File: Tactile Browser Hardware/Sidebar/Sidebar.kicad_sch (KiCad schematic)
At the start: 0 parts

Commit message: I2C
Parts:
- added A1: Arduino_Nano_v3.x, Module:Arduino_Nano, symbol MCU_Module:Arduino_Nano_v3.x
- added Buck_converter: LM2596S-5, Package_TO_SOT_SMD:TO-263-5_TabPin3, symbol Regulator_Switching:LM2596S-5
- added R1, R2: R, symbol Device:R
- added SW1, SW2, SW3, SW4, SW5, SW6, SW7, SW8: SW_Push, symbol Switch:SW_Push
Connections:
- new net 5V: A1.27 (+5V)
- new net GND: A1.29 (GND), A1.4 (GND)
- new net SCL: A1.24 (A5)
- new net SDA: A1.23 (A4)

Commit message: more sidebar progress
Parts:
- removed Buck_converter: LM2596S-5, Package_TO_SOT_SMD:TO-263-5_TabPin3, symbol Regulator_Switching:LM2596S-5
- removed SW8: SW_Push, symbol Switch:SW_Push
- added J1, J2: Conn_01x02_Pin, symbol Connector:Conn_01x02_Pin
- added J3: Barrel_Jack, symbol Connector:Barrel_Jack
- added SW9: RotaryEncoder, symbol Device:RotaryEncoder
- added U1: XL4015, Package_TO_SOT_SMD:TO-263-5_TabPin3, symbol Regulator_Switching:XL4015
- renumbered R1 to 4.7k_ohm, R2 to 4.7k_ohm2, SW2 to Down, SW3 to Left, SW4 to Right, SW1 to Up, SW5 to power_button
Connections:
- net 5V: now also 4.7k_ohm.1, 4.7k_ohm2.2
- net GND: now also SW9.C, U1.1 (GND)
- net SCL: now also 4.7k_ohm2.1, J1.1 (Pin_1)
- net SDA: now also 4.7k_ohm.2, J1.2 (Pin_2)
- net SW5_in: now reaches power_button.1
- net SW5_in: now also A1.19 (A0)
- net SW5_out: now reaches power_button.2
- net SW5_out: now also A1.20 (A1)
- net SW6_in: now reaches SW6.1
- net SW6_in: now also A1.21 (A2)
- net SW6_out: now reaches SW6.2
- net SW6_out: now also A1.22 (A3)
- net SW3_in: now reaches Left.1
- net SW3_in: now also A1.11 (D8)
- net SW3_out: now reaches Left.2
- net SW3_out: now also A1.14 (D11)
- net SW2_out: now reaches A1.10 (D7)
- net SW2_out: now also Down.2
- net PWM1: now reaches A1.12 (D9)
- net PWM1: now also J2.1 (Pin_1)
- net PWM2: now reaches A1.13 (D10)
- net PWM2: now also J2.2 (Pin_2)
- net SW4_in: now reaches A1.15 (D12)
- net SW4_in: now also Right.1
- net SW4_out: now reaches A1.16 (D13)
- net SW4_out: now also Right.2
- net SW7_in: now reaches A1.25 (A6)
- net SW7_in: now also SW7.1
- net SW7_out: now reaches A1.26 (A7)
- net SW7_out: now also SW7.2
- net RE1: now reaches A1.5 (D2)
- net RE1: now also SW9.A
- net RE2: now reaches A1.6 (D3)
- net RE2: now also SW9.B
- net SW1_in: now reaches A1.7 (D4)
- net SW1_in: now also Up.1
- net SW1_out: now reaches A1.8 (D5)
- net SW1_out: now also Up.2
- net SW2_in: now reaches A1.9 (D6)
- net SW2_in: now also Down.1
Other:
- moved on the sheet: 4.7k_ohm, 4.7k_ohm2, Down, Left, Right, SW6, SW7, Up, power_button

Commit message: sidebar progress
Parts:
- added AudioSpeed: RotaryEncoder, symbol Device:RotaryEncoder
- added U2: 74HC595, symbol 74xx:74HC595
- renumbered SW9 to Volume
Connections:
- net 5V: now also U2.10 (~{SRCLR}), U2.16 (VCC)
- net GND: now also AudioSpeed.C, U2.13 (~{OE}), U2.8 (GND)
- net PWM1: now also A1.8 (D5); no longer A1.12 (D9)
- net PWM2: now also A1.12 (D9); no longer A1.13 (D10)
- net SW1_in: now also A1.10 (D7); no longer A1.7 (D4)
- net SW1_out: now also A1.11 (D8); no longer A1.8 (D5)
- net SW2_in: now also A1.19 (A0); no longer A1.9 (D6)
- net SW2_out: now also A1.20 (A1); no longer A1.10 (D7)
- net SW3_in: now also A1.21 (A2); no longer A1.11 (D8)
- net SW3_out: now also A1.22 (A3); no longer A1.14 (D11)
- net SW4_in: now also A1.25 (A6); no longer A1.15 (D12)
- net SW4_out: now also A1.26 (A7); no longer A1.16 (D13)
- net SW5_in: now also U2.15 (QA); no longer A1.19 (A0)
- net SW5_out: now also U2.1 (QB); no longer A1.20 (A1)
- net SW6_in: now also U2.2 (QC); no longer A1.21 (A2)
- net SW6_out: now also U2.3 (QD); no longer A1.22 (A3)
- net SW7_in: now also U2.4 (QE); no longer A1.25 (A6)
- net SW7_out: now also U2.5 (QF); no longer A1.26 (A7)
- net 12V: now reaches U1.5 (VIN)
- new net AS1: A1.7 (D4), AudioSpeed.A
- new net AS2: A1.9 (D6), AudioSpeed.B
- new net CLOCK: A1.16 (D13), U2.11 (SRCLK)
- new net DATA: A1.14 (D11), U2.14 (SER)
- new net LATCH: A1.13 (D10), U2.12 (RCLK)

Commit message: electrical safety
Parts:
- removed J3: Barrel_Jack, symbol Connector:Barrel_Jack
- removed U1: XL4015, Package_TO_SOT_SMD:TO-263-5_TabPin3, symbol Regulator_Switching:XL4015
- added 100k, R220: R, symbol Device:R
- added 6,800-10,000uf: C_US, symbol Device:C_US
- added F_20A: Fuse, symbol Device:Fuse
- added J3: Barrel_Jack_Switch, symbol Connector:Barrel_Jack_Switch
- added Kill_Switch_DC: SW_SPST, symbol Switch:SW_SPST
- added Q1: Q_PMOS_SGD, symbol Transistor_FET:Q_PMOS_SGD
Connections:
- net 12V: now also 6,800-10,000uf.1, Q1.1 (S)
- net GND: now also 6,800-10,000uf.2, J3.2
- net D12_mosfet: now reaches A1.15 (D12)
- net D12_mosfet: now also R220.1
- new net: 100k.1, Q1.2 (G), R220.2
- new net: 100k.2, Kill_Switch_DC.2 (B), Q1.3 (D)
- new net: F_20A.1, J3.1
- new net: F_20A.2, Kill_Switch_DC.1 (A)

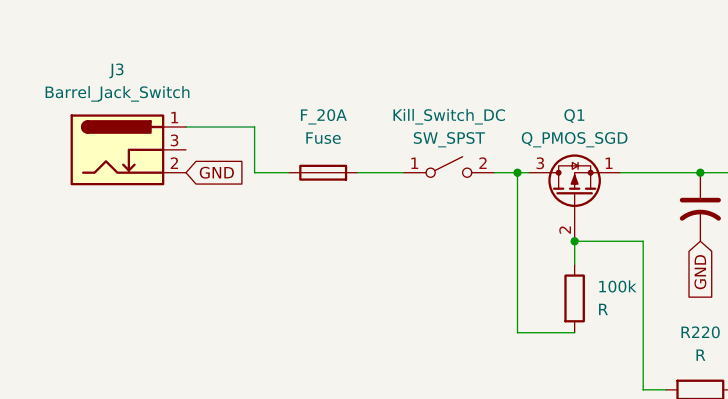
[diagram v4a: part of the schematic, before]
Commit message: updated solenoid/keyswitch connectors
for ease of manufacturing
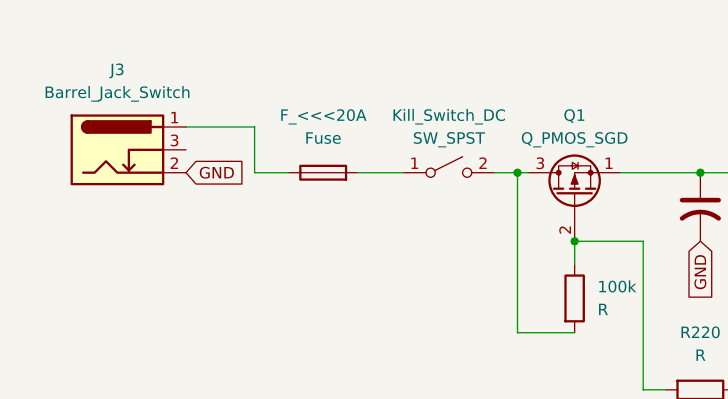
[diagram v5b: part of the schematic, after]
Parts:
- renumbered F_20A to F_<<<20A
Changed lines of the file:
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@@
 		(dnp no)
 		(fields_autoplaced yes)
-		(property "Reference" "F_20A"
+		(property "Reference" "F_<<<20A"
 			(at 45.72 43.18 90)
 			(effects
@@
 			(project ""
 				(path "/16cfaf40-0992-40a8-a734-5ca99128006a"
-					(reference "F_20A")
+					(reference "F_<<<20A")
 					(unit 1)
 				)

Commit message: sidebar updates
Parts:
- removed 100k, R220: R, symbol Device:R
- removed Q1: Q_PMOS_SGD, symbol Transistor_FET:Q_PMOS_SGD
- removed U2: 74HC595, symbol 74xx:74HC595
- added SW10, SW11, SW12, SW8, SW9: SW_Push, symbol Switch:SW_Push
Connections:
- net 12V: now also Kill_Switch_DC.2 (B)
- net SW1_in: no longer A1.10 (D7)
- net SW2_in: no longer A1.19 (A0)
- net SW3_in: no longer A1.21 (A2)
- net SW4_in: no longer A1.25 (A6)
- net CLOCK: no longer names the net of A1.16 (D13)
- net DATA: no longer names the net of A1.14 (D11)
- net LATCH: no longer names the net of A1.13 (D10)
- net SW1_out: no longer names the net of Up.2
- net SW1_out: no longer A1.11 (D8)
- net SW2_out: no longer names the net of A1.20 (A1)
- net SW2_out: no longer Down.2
- net SW3_out: no longer names the net of Left.2
- net SW3_out: no longer A1.22 (A3)
- net SW4_out: no longer names the net of A1.26 (A7)
- net SW4_out: no longer Right.2
- net SW5_in: no longer names the net of power_button.1
- net SW5_out: no longer names the net of power_button.2
- net SW6_in: no longer names the net of SW6.1
- net SW6_out: no longer names the net of SW6.2
- net SW7_in: no longer names the net of SW7.1
- net SW7_out: no longer names the net of SW7.2
- new net Row1: A1.10 (D7)
- new net Row2: A1.11 (D8)
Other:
- moved on the sheet: 4.7k_ohm, 4.7k_ohm2, 6,800-10,000uf, A1, AudioSpeed, Down, F_<<<20A, J1, J2, J3, Kill_Switch_DC, Left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

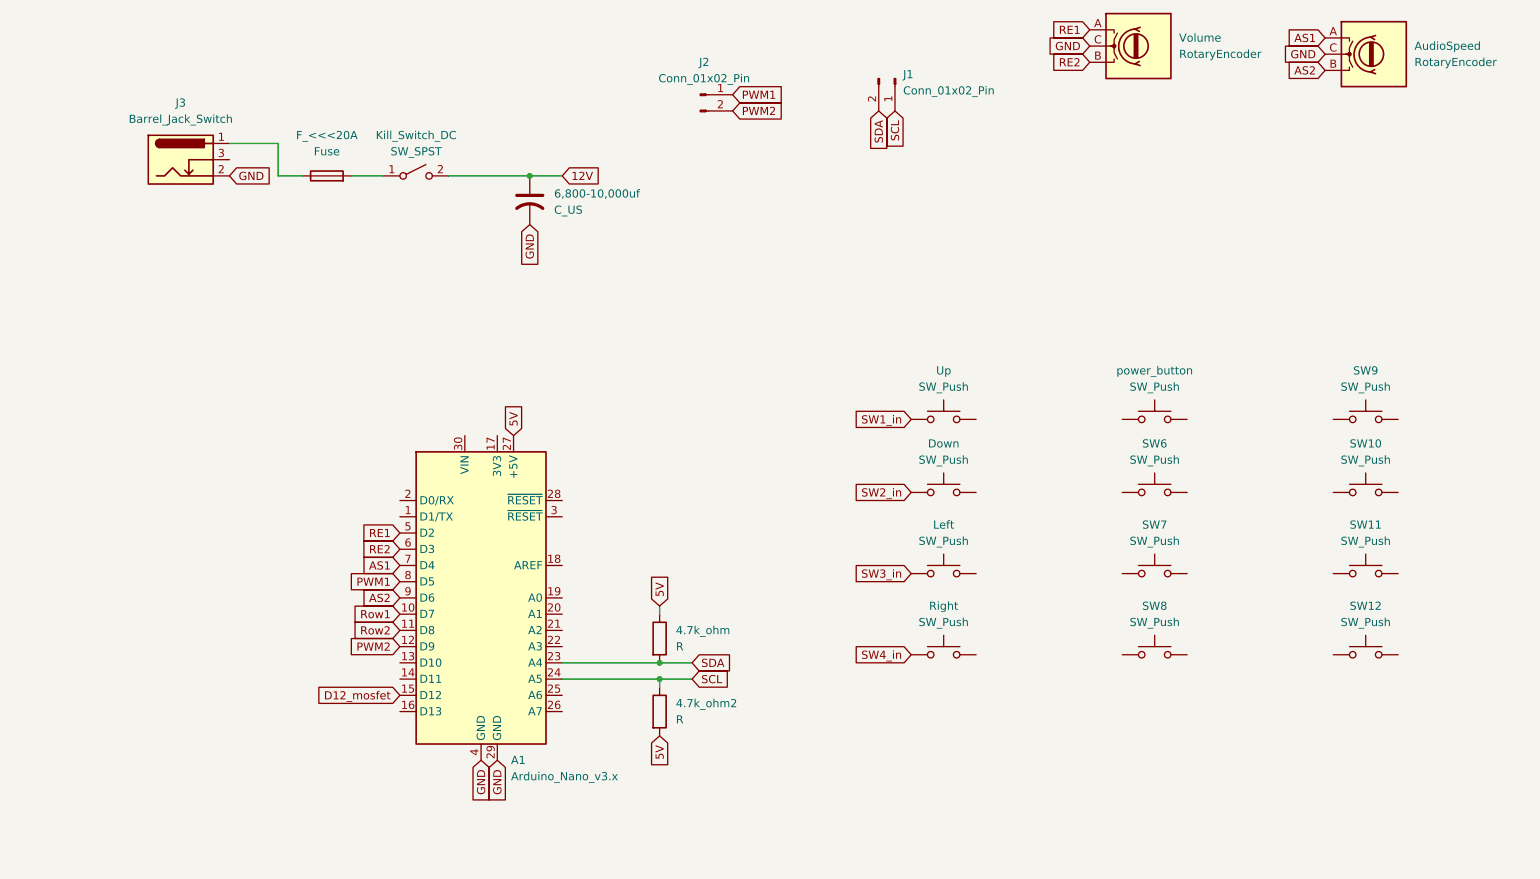
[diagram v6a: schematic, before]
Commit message: finished with sidebar schematic!
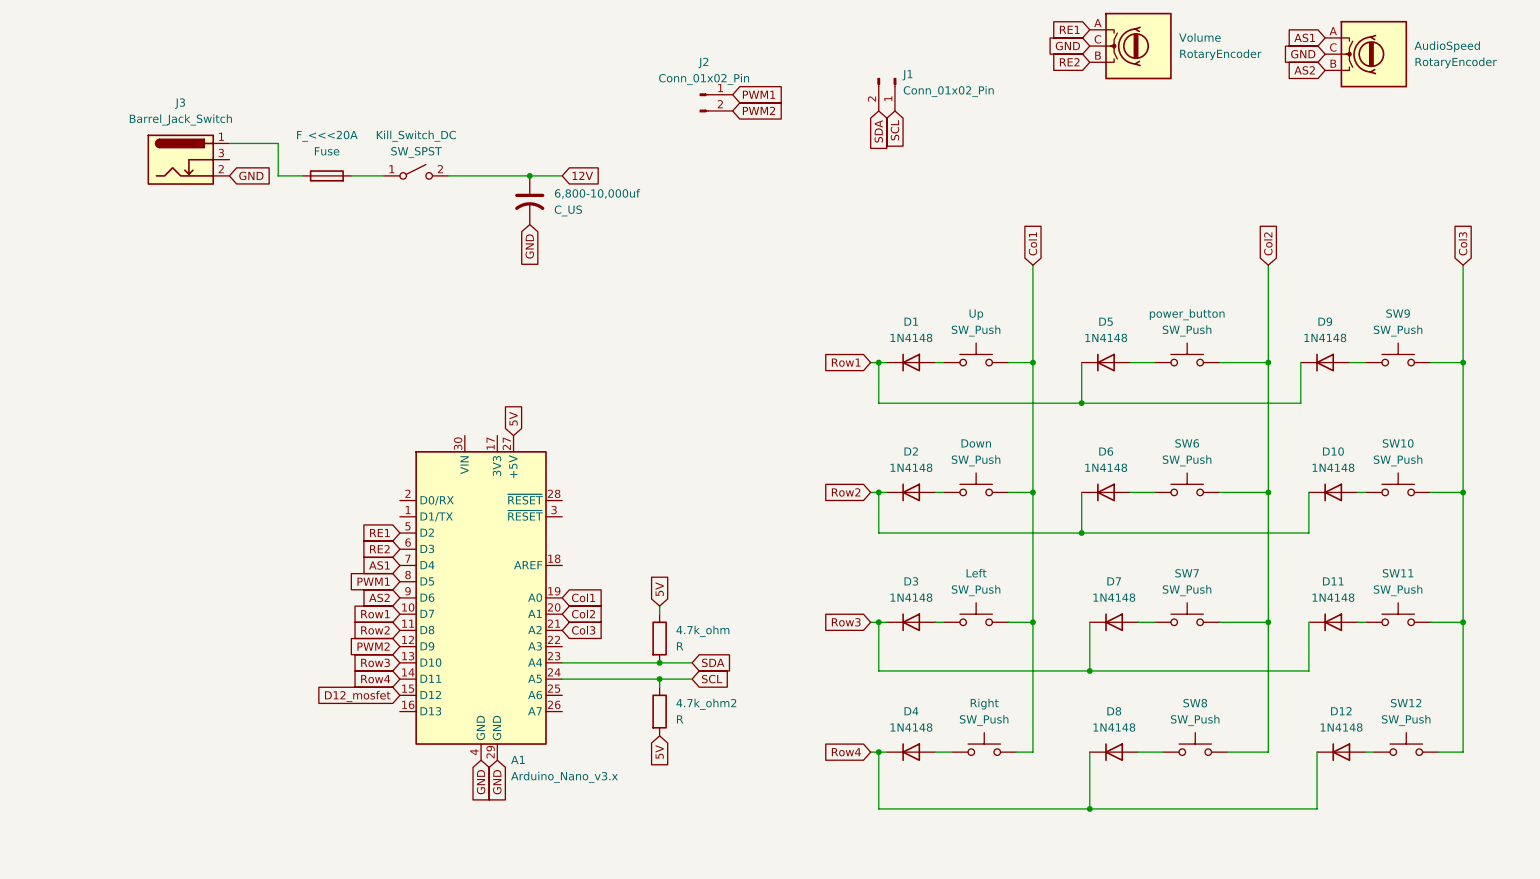
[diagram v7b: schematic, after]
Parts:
- added D1, D10, D11, D12, D2, D3, D4, D5, D6, D7, D8, D9: 1N4148, Diode_THT:D_DO-35_SOD27_P7.62mm_Horizontal, symbol Diode:1N4148
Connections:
- net Row1: now also D1.1 (K), D5.1 (K), D9.1 (K)
- net Row2: now also D10.1 (K), D2.1 (K), D6.1 (K)
- net at power_button.1: now also D5.2 (A)
- net Col2: now reaches power_button.2
- net Col2: now also A1.20 (A1), SW6.2, SW7.2, SW8.2
- net at SW11.1: now also D11.2 (A)
- net Col3: now reaches SW11.2
- net Col3: now also A1.21 (A2), SW10.2, SW12.2, SW9.2
- net at SW6.1: now also D6.2 (A)
- net Col1: now reaches Left.2
- net Col1: now also A1.19 (A0), Down.2, Right.2, Up.2
- net Row3: now reaches A1.13 (D10)
- net Row3: now also D11.1 (K), D3.1 (K), D7.1 (K)
- net Row4: now reaches A1.14 (D11)
- net Row4: now also D12.1 (K), D4.1 (K), D8.1 (K)
- net at SW10.1: now also D10.2 (A)
- net at SW12.1: now also D12.2 (A)
- net at SW8.1: now also D8.2 (A)
- net at SW7.1: now also D7.2 (A)
- net at SW9.1: now also D9.2 (A)
- net SW1_in: no longer names the net of Up.1
- net SW1_in: now also D1.2 (A)
- net SW2_in: no longer names the net of Down.1
- net SW2_in: now also D2.2 (A)
- net SW3_in: no longer names the net of Left.1
- net SW3_in: now also D3.2 (A)
- net SW4_in: no longer names the net of Right.1
- net SW4_in: now also D4.2 (A)
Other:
- moved on the sheet: Down, Left, Right, SW10, SW11, SW12, SW6, SW7, SW8, SW9, Up, power_button

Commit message: finished footprints (mostly)
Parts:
- added 1000uf25V1, 1000uf25V2: C_US, Capacitor_SMD:CP_Elec_10x12.5, symbol Device:C_US
- added J4: Conn_01x02_Pin, Connector_JST:JST_PH_B2B-PH-SM4-TB_1x02-1MP_P2.00mm_Vertical, symbol Connector:Conn_01x02_Pin
- 1000uf25V3: renamed from 6,800-10,000uf; footprint (none) -> Capacitor_SMD:CP_Elec_10x12.5
- 4.7k_ohm1: renamed from 4.7k_ohm; footprint (none) -> Resistor_SMD:R_0402_1005Metric
- 4.7k_ohm2: footprint (none) -> Resistor_SMD:R_0402_1005Metric
- AudioSpeed1: renamed from AudioSpeed; footprint (none) -> Rotary_Encoder:RotaryEncoder_Bourns_Horizontal_PEC12R-2x17F-Sxxxx
- D1, D10, D11, D12, D2, D3, D4, D5, D6, D7, D8, D9: footprint Diode_THT:D_DO-35_SOD27_P7.62mm_Horizontal -> Diode_SMD:D_SOD-123
- Down1: renamed from Down; footprint (none) -> Button_Switch_SMD:SW_SPST_EVQQ2
- Fuse1: renamed from F_<<<20A; footprint (none) -> Fuse:Fuse_0402_1005Metric_Pad0.77x0.64mm_HandSolder
- J1: footprint (none) -> Connector_JST:JST_PH_B2B-PH-SM4-TB_1x02-1MP_P2.00mm_Vertical
- J2: footprint (none) -> TerminalBlock_MetzConnect:TerminalBlock_MetzConnect_Type011_RT05503HBLC_1x03_P5.00mm_Horizontal
- J3: footprint (none) -> Connector_BarrelJack:BarrelJack_CUI_PJ-063AH_Horizontal
- Kill_Switch_DC1: renamed from Kill_Switch_DC; footprint (none) -> Button_Switch_Keyboard:SW_Cherry_MX_1.00u_PCB
- Left1: renamed from Left; footprint (none) -> Button_Switch_SMD:SW_SPST_EVQQ2
- Right1: renamed from Right; footprint (none) -> Button_Switch_SMD:SW_SPST_EVQQ2
- SW10, SW11, SW12, SW6, SW7, SW8, SW9: footprint (none) -> Button_Switch_SMD:SW_SPST_EVQQ2
- Up1: renamed from Up; footprint (none) -> Button_Switch_SMD:SW_SPST_EVQQ2
- Volume1: renamed from Volume; footprint (none) -> Rotary_Encoder:RotaryEncoder_Bourns_Horizontal_PEC12R-2x17F-Sxxxx
- power_button1: renamed from power_button; footprint (none) -> Button_Switch_SMD:SW_SPST_EVQQ2
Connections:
- net 12V: now also J2.1 (Pin_1), 1000uf25V1.1, 1000uf25V2.1
- net 5V: now also J4.1 (Pin_1)
- net GND: now also J2.2 (Pin_2), 1000uf25V1.2, 1000uf25V2.2, J4.2 (Pin_2)
- net PWM1: no longer J2.1 (Pin_1)
- net PWM2: no longer J2.2 (Pin_2)
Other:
- moved on the sheet: 1000uf25V3
